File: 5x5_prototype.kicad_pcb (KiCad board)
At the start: 2 copper layers, 50 x 50 mm, 104 parts, among them CON1 USB-MINI-B, CON2 BARREL_JACK, CON3 USB-MINI-B, J1 INTERCONNECT_2, J10 INTERCONNECT_3, J11 INTERCONNECT_3, J12 INTERCONNECT_3, J13 INTERCONNECT_3, J14 INTERCONNECT_3, J15 INTERCONNECT_3, J16 INTERCONNECT_3, J17 INTERCONNECT_3, J18 INTERCONNECT_3, J19 INTERCONNECT_4, J2 INTERCONNECT_16_2_16, J20 INTERCONNECT_5, J21 INTERCONNECT_16, J22 INTERCONNECT_3, J23 INTERCONNECT_3, J24 INTERCONNECT_3, J25 INTERCONNECT_3, J26 INTERCONNECT_3, J27 INTERCONNECT_3, J28 INTERCONNECT_3, J29 INTERCONNECT_3, J3 INTERCONNECT_3, J30 INTERCONNECT_3, J31 INTERCONNECT_3, J32 INTERCONNECT_3, J33 INTERCONNECT_3, J34 INTERCONNECT_3, J35 INTERCONNECT_3, J36 INTERCONNECT_3, J37 INTERCONNECT_3, J38 INTERCONNECT_16, J39 INTERCONNECT_6, J4 INTERCONNECT_3, J40 INTERCONNECT_7, J41 INTERCONNECT_3, J42 INTERCONNECT_3, J43 INTERCONNECT_3, J44 INTERCONNECT_3, J45 INTERCONNECT_3, J46 INTERCONNECT_3, J47 INTERCONNECT_3, J48 INTERCONNECT_3, J49 INTERCONNECT_3, J5 INTERCONNECT_3, J50 INTERCONNECT_3, J51 INTERCONNECT_3, J52 INTERCONNECT_3, J53 INTERCONNECT_3, J54 INTERCONNECT_3, J55 INTERCONNECT_3, J56 INTERCONNECT_3, J57 INTERCONNECT_3, J58 INTERCONNECT_3, J59 INTERCONNECT_3, J6 INTERCONNECT_3, J60 INTERCONNECT_3, J61 INTERCONNECT_3, J62 INTERCONNECT_3, J63 INTERCONNECT_3, J64 INTERCONNECT_3, J65 INTERCONNECT_3, J66 INTERCONNECT_3, J67 INTERCONNECT_3, J68 INTERCONNECT_3, J69 INTERCONNECT_3, J7 INTERCONNECT_3, J70 INTERCONNECT_3, J71 INTERCONNECT_3, J72 INTERCONNECT_3, J8 INTERCONNECT_3, J9 INTERCONNECT_3, P1 CONN_5, U1 7805

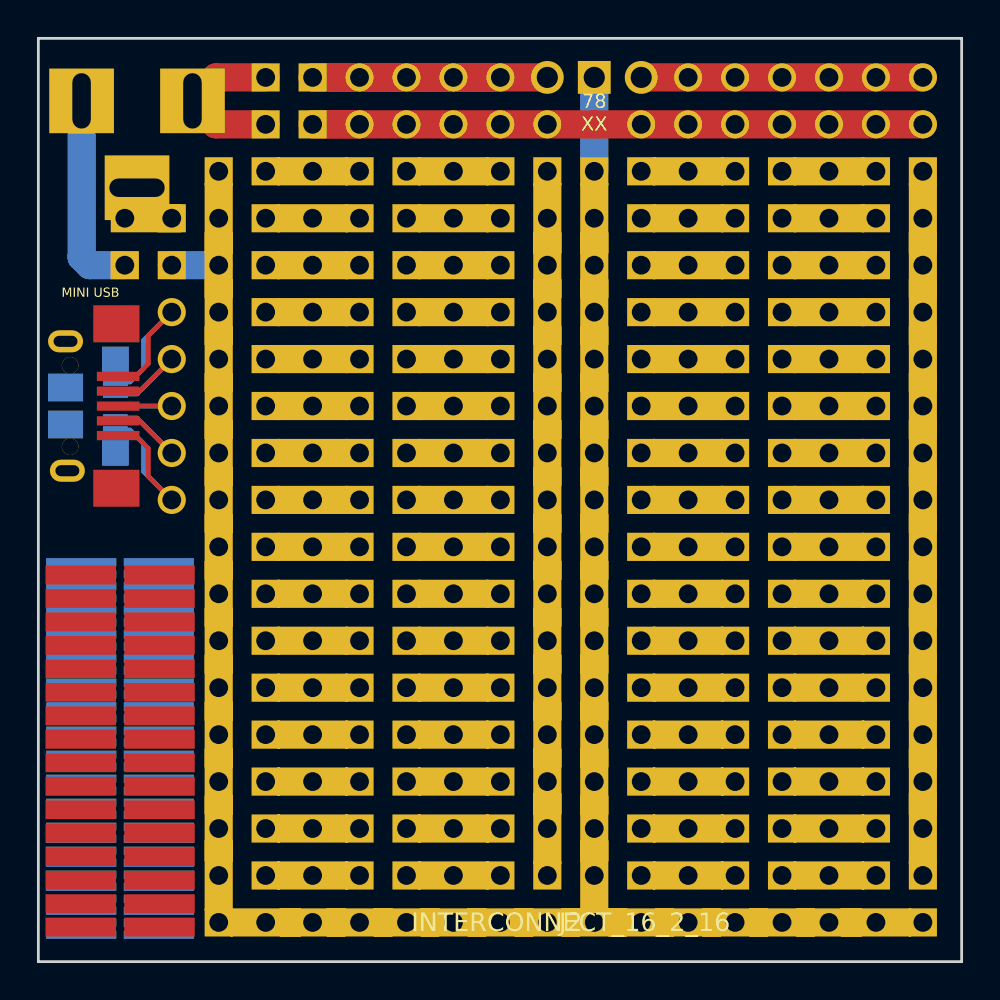
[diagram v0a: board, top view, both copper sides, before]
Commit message: fixed SMD pin spacing and pad width
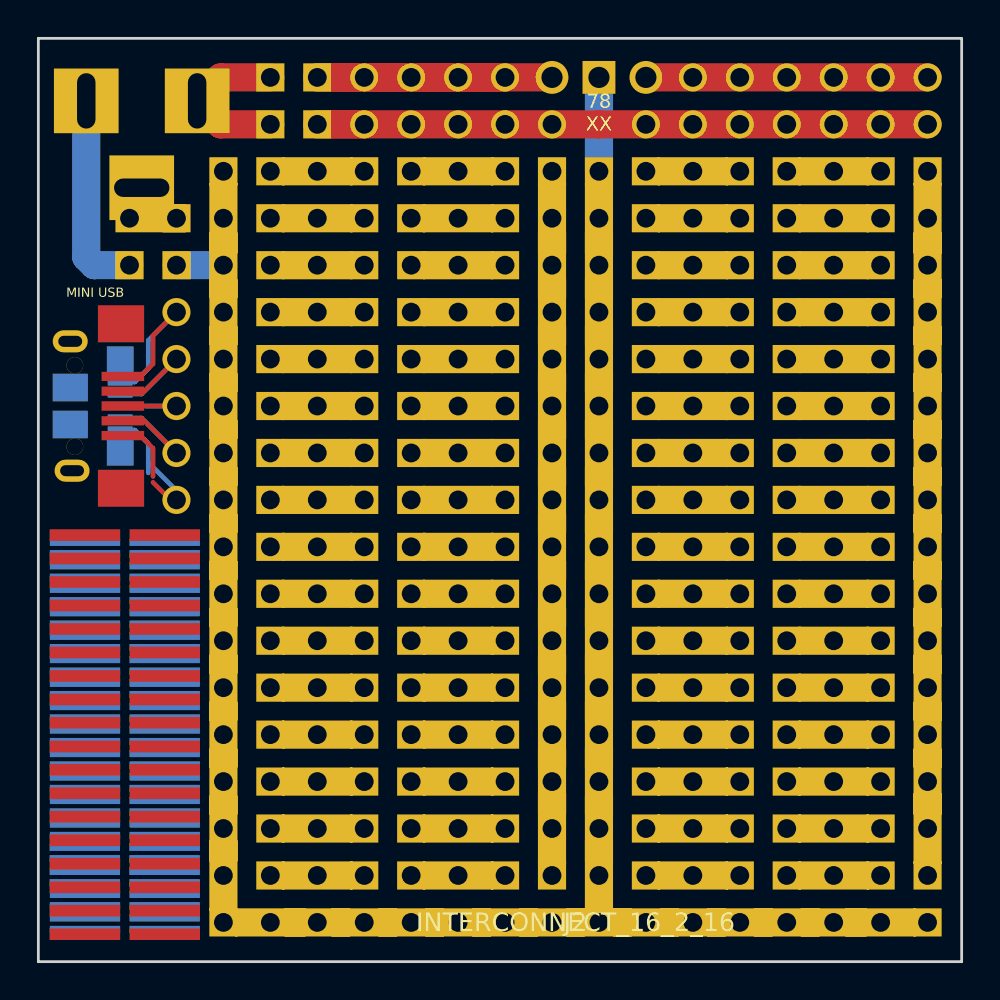
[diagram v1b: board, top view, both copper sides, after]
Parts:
- added ?: , SMD_127_380_2X2, F.Cu at (149.9, 163.2)
- added ?: , SMD_065_38_2X2, B.Cu at (149.9, 162.3)
- ? (x8): footprint SMD_127_3_2X2 -> SMD_127_380_2X2
- moved ? 0.46 mm to (149.9, 183.5)
- moved ? 0.46 mm to (149.9, 181.0)
- moved ? 0.46 mm to (149.9, 178.4)
- moved ? 0.46 mm to (149.9, 175.9)
- moved ? 0.46 mm to (149.9, 173.4)
- moved ? 0.46 mm to (149.9, 170.8)
- moved ? 0.46 mm to (149.9, 168.3)
- moved ? 0.46 mm to (149.9, 165.7)
- moved ? 0.38 mm to (149.9, 182.6)
- moved ? 0.36 mm to (149.9, 181.4)
- moved ? 0.32 mm to (149.9, 180.1)
- moved ? 0.32 mm to (149.9, 178.8)
- moved ? 0.31 mm to (149.9, 163.6)
- moved ? 0.30 mm to (149.9, 177.5)
- moved ? 0.30 mm to (149.9, 164.8)
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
